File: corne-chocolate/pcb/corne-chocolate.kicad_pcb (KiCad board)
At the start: 2 copper layers, 133.8 x 91.4 mm, 118 parts, among them J1 MJ-4PP-9, J2 nice!view, J3 Battery, J4 Battery, SW1 SW_Push, SW10 SW_Push, SW11 SW_Push, SW12 SW_Push, SW13 SW_Push, SW14 SW_Push, SW15 SW_Push, SW16 SW_Push, SW17 SW_Push, SW18 SW_Push, SW19 SW_Push, SW2 SW_Push, SW20 SW_Push, SW21 SW_PUSH, SW22 SW_PUSH, SW23 SW_SPDT, SW24 SW_SPDT, SW3 SW_Push, SW4 SW_Push, SW5 SW_Push, SW6 SW_Push, SW7 SW_Push, SW8 SW_Push, SW9 SW_Push, U1 ProMicro

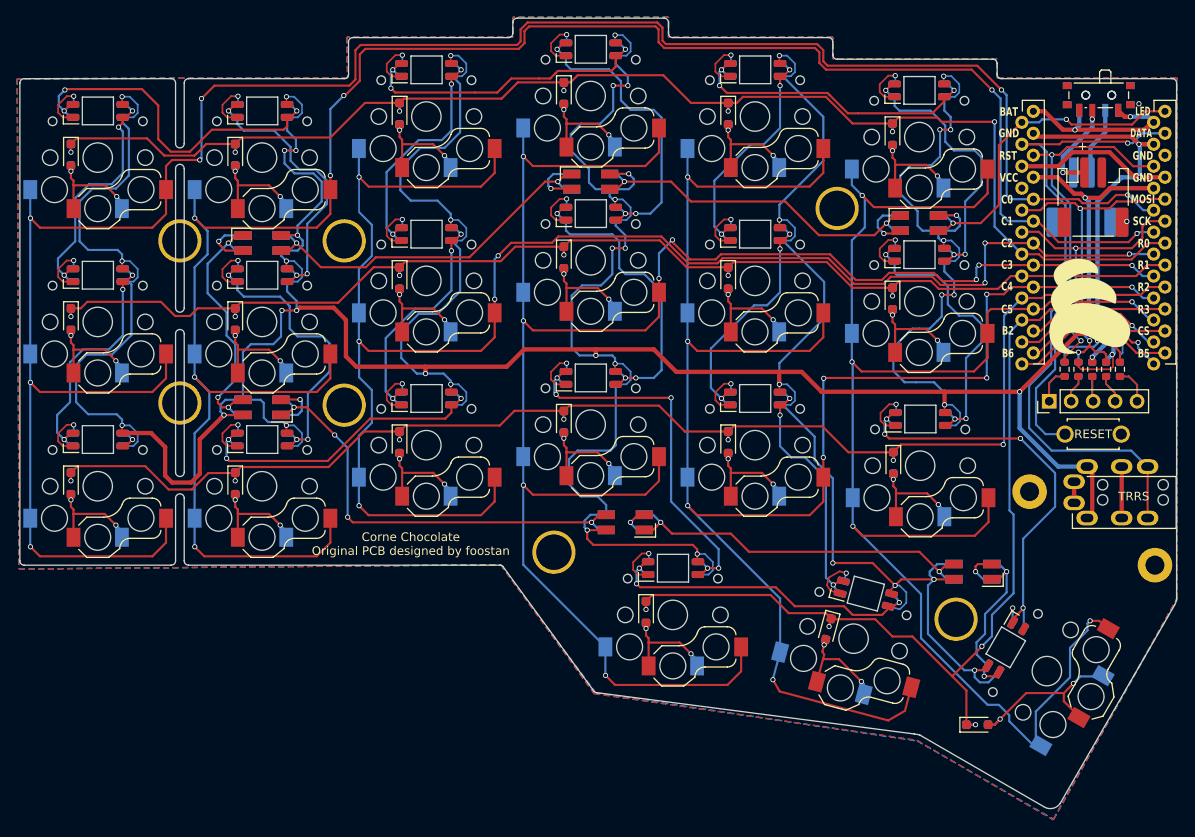
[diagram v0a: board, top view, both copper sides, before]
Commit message: pcb change on/off switch
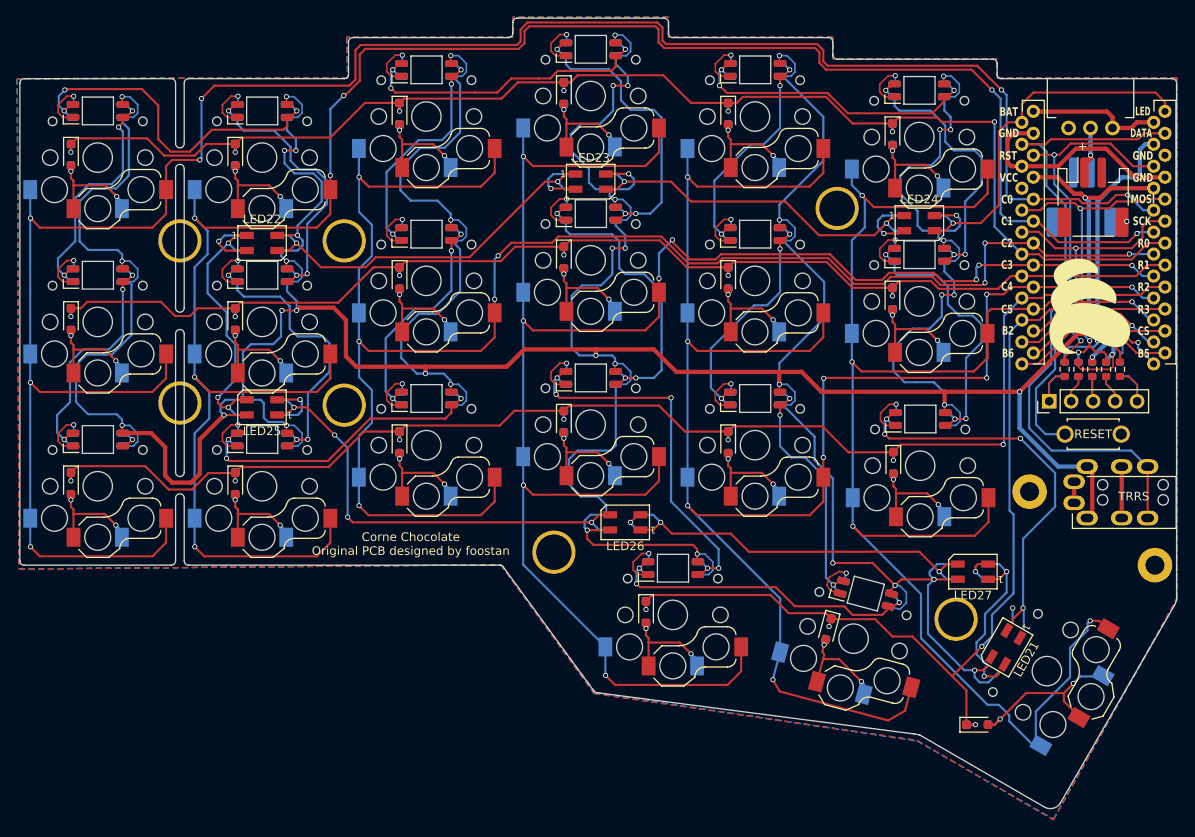
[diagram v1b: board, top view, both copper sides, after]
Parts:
- removed SW24: SW_SPDT, Button_Switch_SMD:SW_SPDT_PCM12
- D1, D10, D11, D13, D14, D15, D2, D21, D22, D23, D24, D25, D26, D27, D28, D29, D3, D30, D31, D32, D33, D34, D35, D36, D37, D38, D39, D4, D40, D41, D42, D43, D44, D45, D46, D47, D48, D5, D6, D7, D8, D9: value D -> 1N4148
- LED21: footprint corne-chocolate:SK6812MINI-E_doublesided -> LED_SMD:LED_SK6812MINI_PLCC4_3.5x3.5mm_P1.75mm
- LED22: renamed from L22; footprint corne-chocolate:SK6812MINI_underglow_rev -> LED_SMD:LED_SK6812MINI_PLCC4_3.5x3.5mm_P1.75mm
- LED23: renamed from L23; footprint corne-chocolate:SK6812MINI_underglow_rev -> LED_SMD:LED_SK6812MINI_PLCC4_3.5x3.5mm_P1.75mm
- LED24: renamed from L24; footprint corne-chocolate:SK6812MINI_underglow_rev -> LED_SMD:LED_SK6812MINI_PLCC4_3.5x3.5mm_P1.75mm
- LED25: renamed from L25; footprint corne-chocolate:SK6812MINI_underglow_rev -> LED_SMD:LED_SK6812MINI_PLCC4_3.5x3.5mm_P1.75mm
- LED26: renamed from L26; footprint corne-chocolate:SK6812MINI_underglow_rev -> LED_SMD:LED_SK6812MINI_PLCC4_3.5x3.5mm_P1.75mm
- LED27: renamed from L27; footprint corne-chocolate:SK6812MINI_underglow_rev -> LED_SMD:LED_SK6812MINI_PLCC4_3.5x3.5mm_P1.75mm
- SW1, SW10, SW11, SW12, SW13, SW14, SW15, SW16, SW17, SW18, SW19, SW2, SW20, SW3, SW4, SW5, SW6, SW7, SW8, SW9: value SW_Push -> 1U
- SW21: value SW_PUSH -> 1.5U
- SW23: footprint Button_Switch_SMD:SW_SPDT_PCM12 -> corne-chocolate:ECE_ESP2010
- moved SW23 3.60 mm to (184.8, 73.7), turned to 180 degrees
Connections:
- net /L0 renamed Net-(LED21-DIN)
- J1 pad A: unconnected-(J1-PadA) -> (no net)
- J1 pad B: data -> (no net)
- J1 pad C: GND -> (no net)
- J1 pad D: VCC -> (no net)
- J3 pad 1: Net-(J3-Pin_1) -> Net-(J3-+)
- J3 pad MP: GND -> (no net)
- J4 pad 1: Net-(J4-Pin_1) -> Net-(J3-+)
- J4 pad MP: GND -> (no net)
- SW23 pad 2: Net-(J3-Pin_1) -> Net-(J3-+)
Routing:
- net (no net): track 0.00 -> 55.8 mm, vias 0 -> 2
- net unconnected-(U1-9/PB5-Pad12)_1: track 19.5 -> 0.00 mm
- net unconnected-(U1-10/PB6-Pad13): track 17.7 -> 0.00 mm, vias 1 -> 0
- net unconnected-(U1-16/PB2-Pad14): track 16.1 -> 0.00 mm, vias 1 -> 0
- net Net-(J4-Pin_1): track 11.1 -> 0.00 mm, vias 2 -> 0
- net Net-(J3-Pin_1): track 7.89 -> 0.00 mm
- net Net-(J3-+): track 0.00 -> 7.44 mm, vias 0 -> 1
- net GND: track 234.7 -> 228.0 mm, vias 32 -> 30
- net /Vbat: track 22.3 -> 15.7 mm, vias 2 -> 0
- net LED: track 38.5 -> 42.6 mm, vias 2 -> 1
- net unconnected-(J1-PadA): track 2.45 -> 0.00 mm
- net data: track 76.6 -> 76.5 mm, vias 1 -> 0

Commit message: pcb remove TRRS
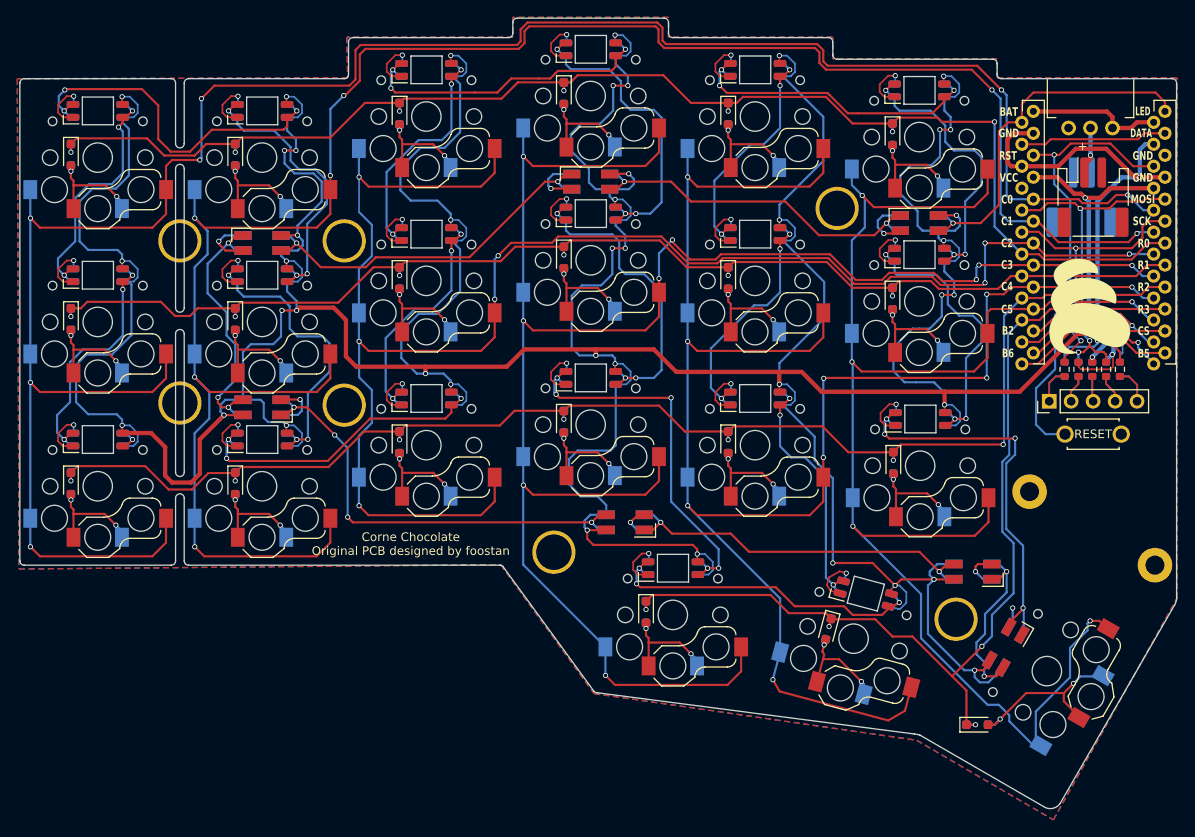
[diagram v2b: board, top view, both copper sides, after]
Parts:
- removed J1: MJ-4PP-9, corne-chocolate:MJ-4PP-9
- LED21, LED22, LED23, LED24, LED25, LED26, LED27: footprint LED_SMD:LED_SK6812MINI_PLCC4_3.5x3.5mm_P1.75mm -> corne-chocolate:SK6812MINI_underglow_rev
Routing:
- net data: track 76.5 -> 17.1 mm
- net VCC: track 732.3 -> 712.0 mm, vias 46 -> 45
- net GND: track 228.0 -> 220.4 mm, vias 30 -> 28
- net (no net): track 55.8 -> 53.3 mm
- net /L1: track 48.0 -> 47.2 mm, vias 4 -> 5
- net row3: track 113.8 -> 114.6 mm
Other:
- board text removed: "TRRS"

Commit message: pcb clean up layout under MCU
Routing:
- net (no net): track 53.3 -> 0.00 mm, vias 2 -> 0
- net unconnected-(U1-16/PB2-Pad14): track 0.00 -> 0.61 mm
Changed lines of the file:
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@@
 	)
 	(segment
-		(start 187.3 96.2)
-		(end 182.3 96.2)
-		(width 0.25)
-		(layer "F.Cu")
-		(net 0)
-	)
-	(segment
-		(start 178.718 100.982)
-		(end 182.9 96.8)
-		(width 0.25)
-		(layer "F.Cu")
-		(net 0)
-	)
-	(segment
-		(start 188.2525 95.2)
-		(end 181 95.2)
-		(width 0.25)
-		(layer "F.Cu")
-		(net 0)
-	)
-	(segment
-		(start 190.112 99.712)
-		(end 193.4064 99.712)
-		(width 0.25)
-		(layer "F.Cu")
-		(net 0)
-	)
-	(segment
-		(start 182.3 96.2)
-		(end 178.788 99.712)
-		(width 0.25)
-		(layer "F.Cu")
-		(net 0)
-	)
-	(segment
-		(start 190.3 98.5)
-		(end 189.6 98.5)
-		(width 0.25)
-		(layer "F.Cu")
-		(net 0)
-	)
-	(segment
-		(start 187.2 96.8)
-		(end 190.112 99.712)
-		(width 0.25)
-		(layer "F.Cu")
-		(net 0)
-	)
-	(segment
-		(start 179.028 97.172)
-		(end 178.1864 97.172)
-		(width 0.25)
-		(layer "F.Cu")
-		(net 0)
-	)
-	(segment
-		(start 189.6 98.5)
-		(end 187.3 96.2)
-		(width 0.25)
-		(layer "F.Cu")
-		(net 0)
-	)
-	(segment
-		(start 178.788 99.712)
-		(end 178.1864 99.712)
-		(width 0.25)
-		(layer "F.Cu")
-		(net 0)
-	)
-	(segment
-		(start 176.86 100.982)
-		(end 178.718 100.982)
-		(width 0.25)
-		(layer "F.Cu")
-		(net 0)
-	)
-	(segment
-		(start 182.9 96.8)
-		(end 187.2 96.8)
-		(width 0.25)
-		(layer "F.Cu")
-		(net 0)
-	)
-	(segment
-		(start 181 95.2)
-		(end 179.028 97.172)
-		(width 0.25)
-		(layer "F.Cu")
-		(net 0)
-	)
-	(segment
-		(start 189.6 96.5475)
-		(end 188.2525 95.2)
-		(width 0.25)
-		(layer "F.Cu")
-		(net 0)
-	)
-	(via
-		(at 189.6 96.5475)
-		(size 0.6)
-		(drill 0.4)
-		(layers "F.Cu" "B.Cu")
-		(net 0)
-	)
-	(via
-		(at 190.3 98.5)
-		(size 0.6)
-		(drill 0.4)
-		(layers "F.Cu" "B.Cu")
-		(net 0)
-	)
-	(segment
-		(start 190.3 98.5)
-		(end 190.3 99.1)
-		(width 0.25)
-		(layer "B.Cu")
-		(net 0)
-	)
-	(segment
-		(start 192.1 100.9)
-		(end 192.1 100.982)
-		(width 0.25)
-		(layer "B.Cu")
-		(net 0)
-	)
-	(segment
-		(start 191.4945 98.442)
-		(end 192.1 98.442)
-		(width 0.25)
-		(layer "B.Cu")
-		(net 0)
-	)
-	(segment
-		(start 190.3 99.1)
-		(end 192.1 100.9)
-		(width 0.25)
-		(layer "B.Cu")
-		(net 0)
-	)
-	(segment
-		(start 189.6 96.5475)
-		(end 191.4945 98.442)
-		(width 0.25)
-		(layer "B.Cu")
-		(net 0)
-	)
-	(segment
 		(start 142.9 70.8)
 		(end 142.9 71.75)
@@
 		(net 75)
 	)
+	(segment
+		(start 192.1 100.9)
+		(end 192.1 100.982)
+		(width 0.25)
+		(layer "B.Cu")
+		(net 76)
+	)
+	(segment
+		(start 191.4945 98.442)
+		(end 192.1 98.442)
+		(width 0.25)
+		(layer "B.Cu")
+		(net 78)
+	)
 	(zone

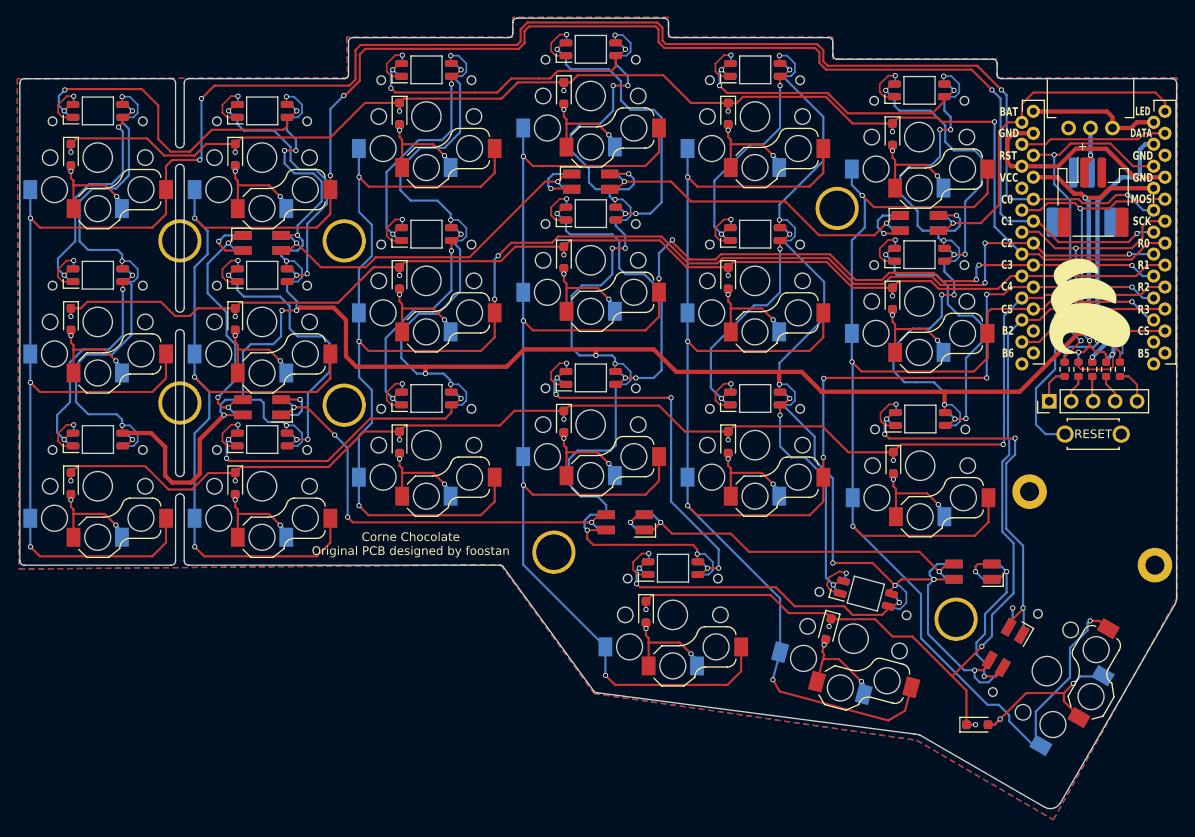
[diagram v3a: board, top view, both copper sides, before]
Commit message: pcb remove underglow LEDs
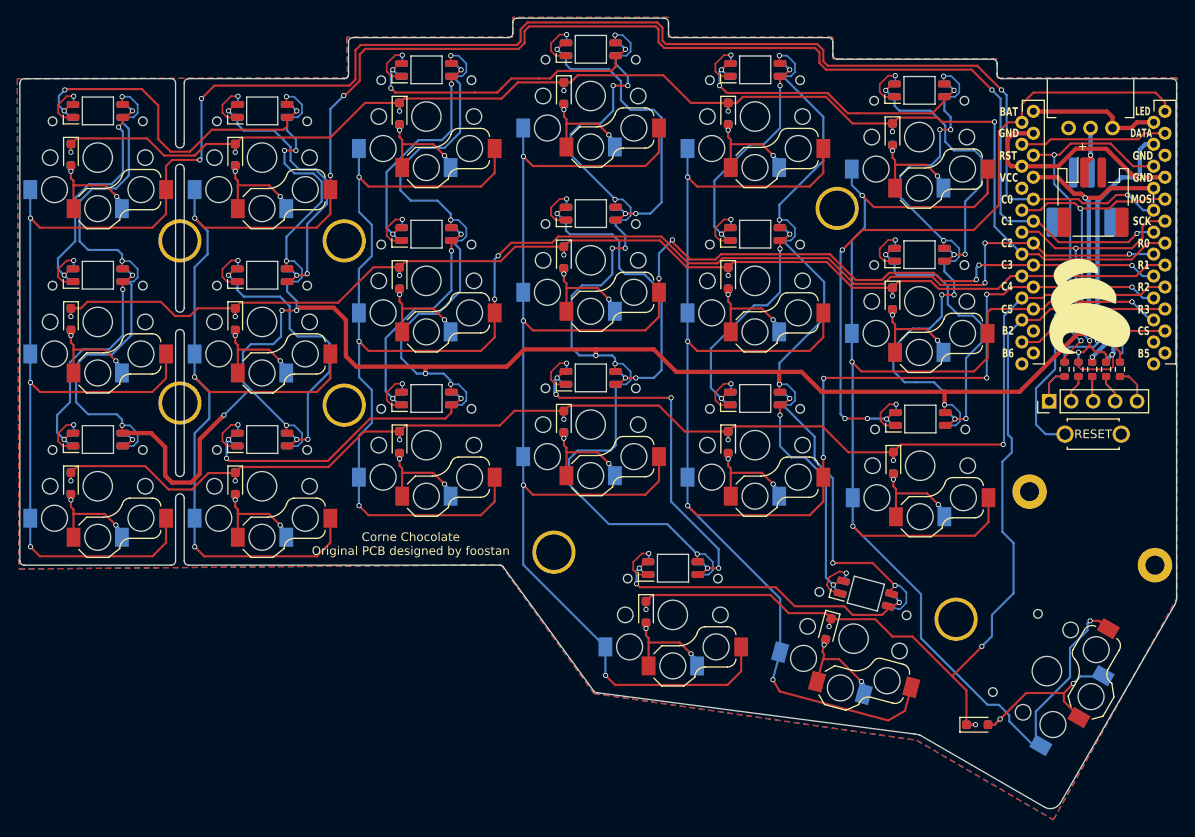
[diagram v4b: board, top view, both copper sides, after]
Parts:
- removed LED21, LED22, LED23, LED24, LED25, LED26, LED27: SK6812MINI, corne-chocolate:SK6812MINI_underglow_rev
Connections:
- LED18 pad 2: /L1 -> LED
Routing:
- net VCC: track 712.0 -> 648.0 mm, vias 45 -> 39
- net Net-(LED25-DOUT): track 52.5 -> 0.00 mm, vias 4 -> 0
- net /L1: track 47.2 -> 0.00 mm, vias 5 -> 0
- net Net-(LED22-DIN): track 43.8 -> 0.00 mm, vias 2 -> 0
- net Net-(LED26-DOUT): track 43.2 -> 0.00 mm, vias 2 -> 0
- net Net-(LED23-DIN): track 41.5 -> 0.00 mm, vias 2 -> 0
- net LED: track 42.6 -> 80.0 mm, vias 1 -> 4
- net GND: track 220.4 -> 185.5 mm, vias 28 -> 22
- net Net-(LED22-DOUT): track 31.3 -> 0.00 mm, vias 3 -> 0
- net Net-(LED21-DIN): track 20.4 -> 0.00 mm, vias 2 -> 0
